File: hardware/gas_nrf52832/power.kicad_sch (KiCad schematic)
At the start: 31 parts, among them IC1 NPM1100-QDAA-R, J2 USB4515-GF-A_REVA, J3 Batt_SW, Q1 DMC2400UV

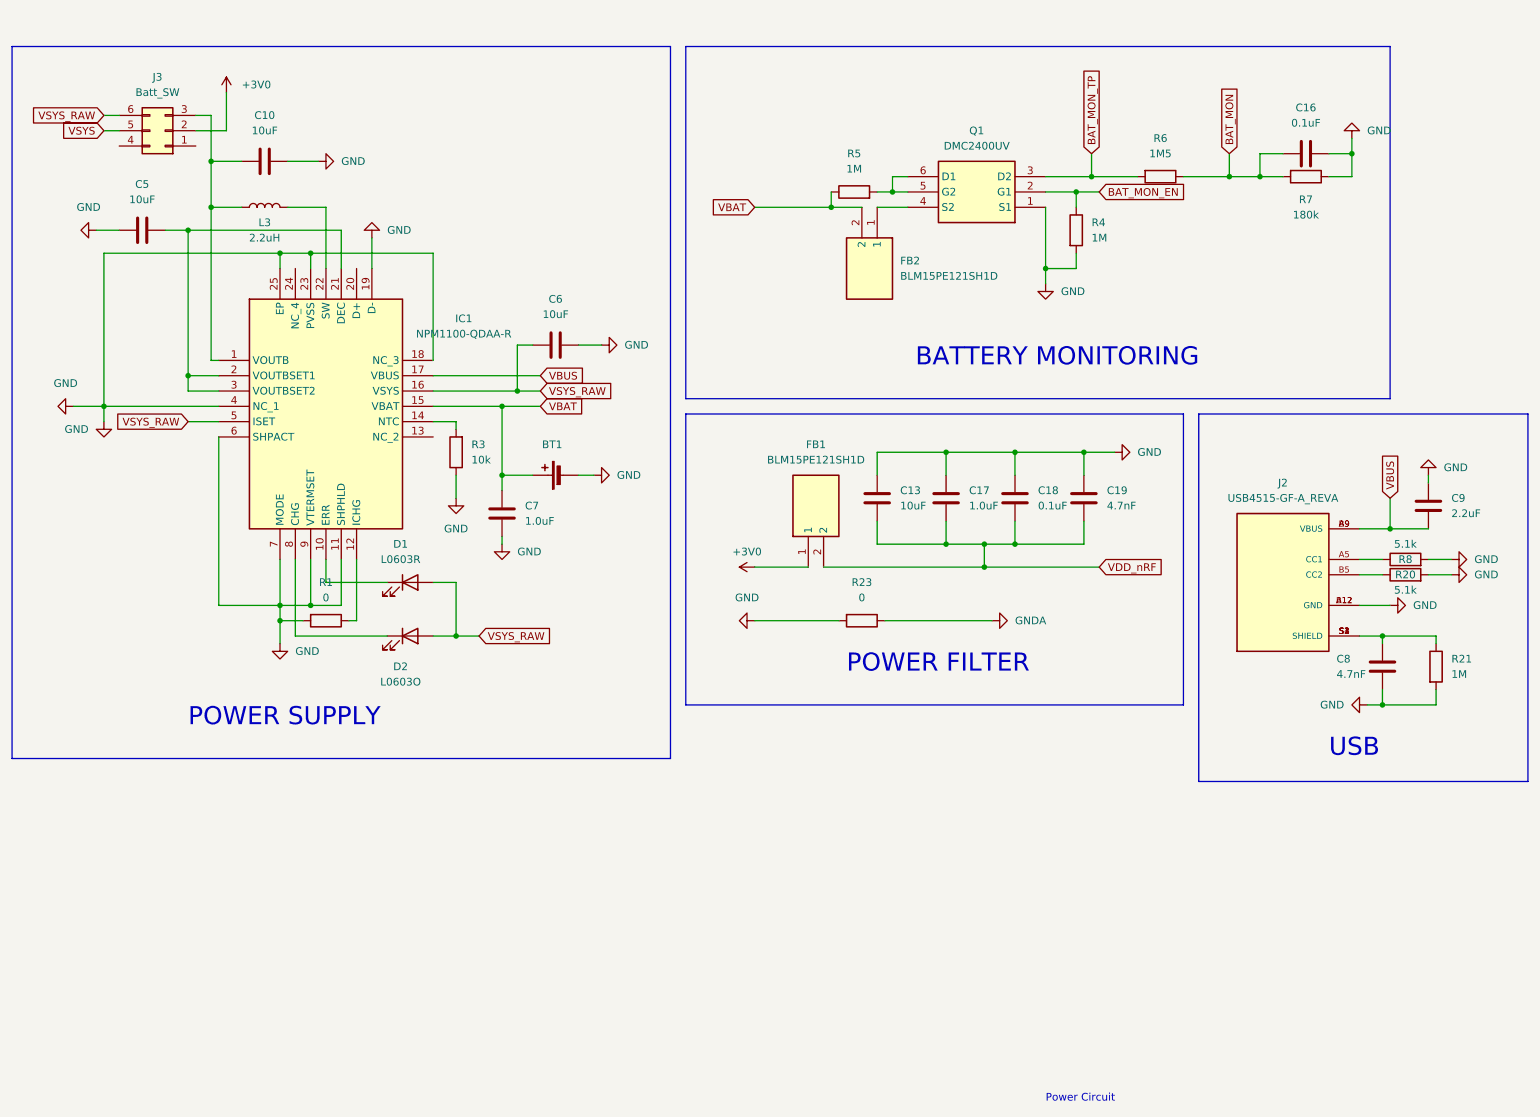
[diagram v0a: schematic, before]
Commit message: hw: fix sensor circuit & fix ERC Error
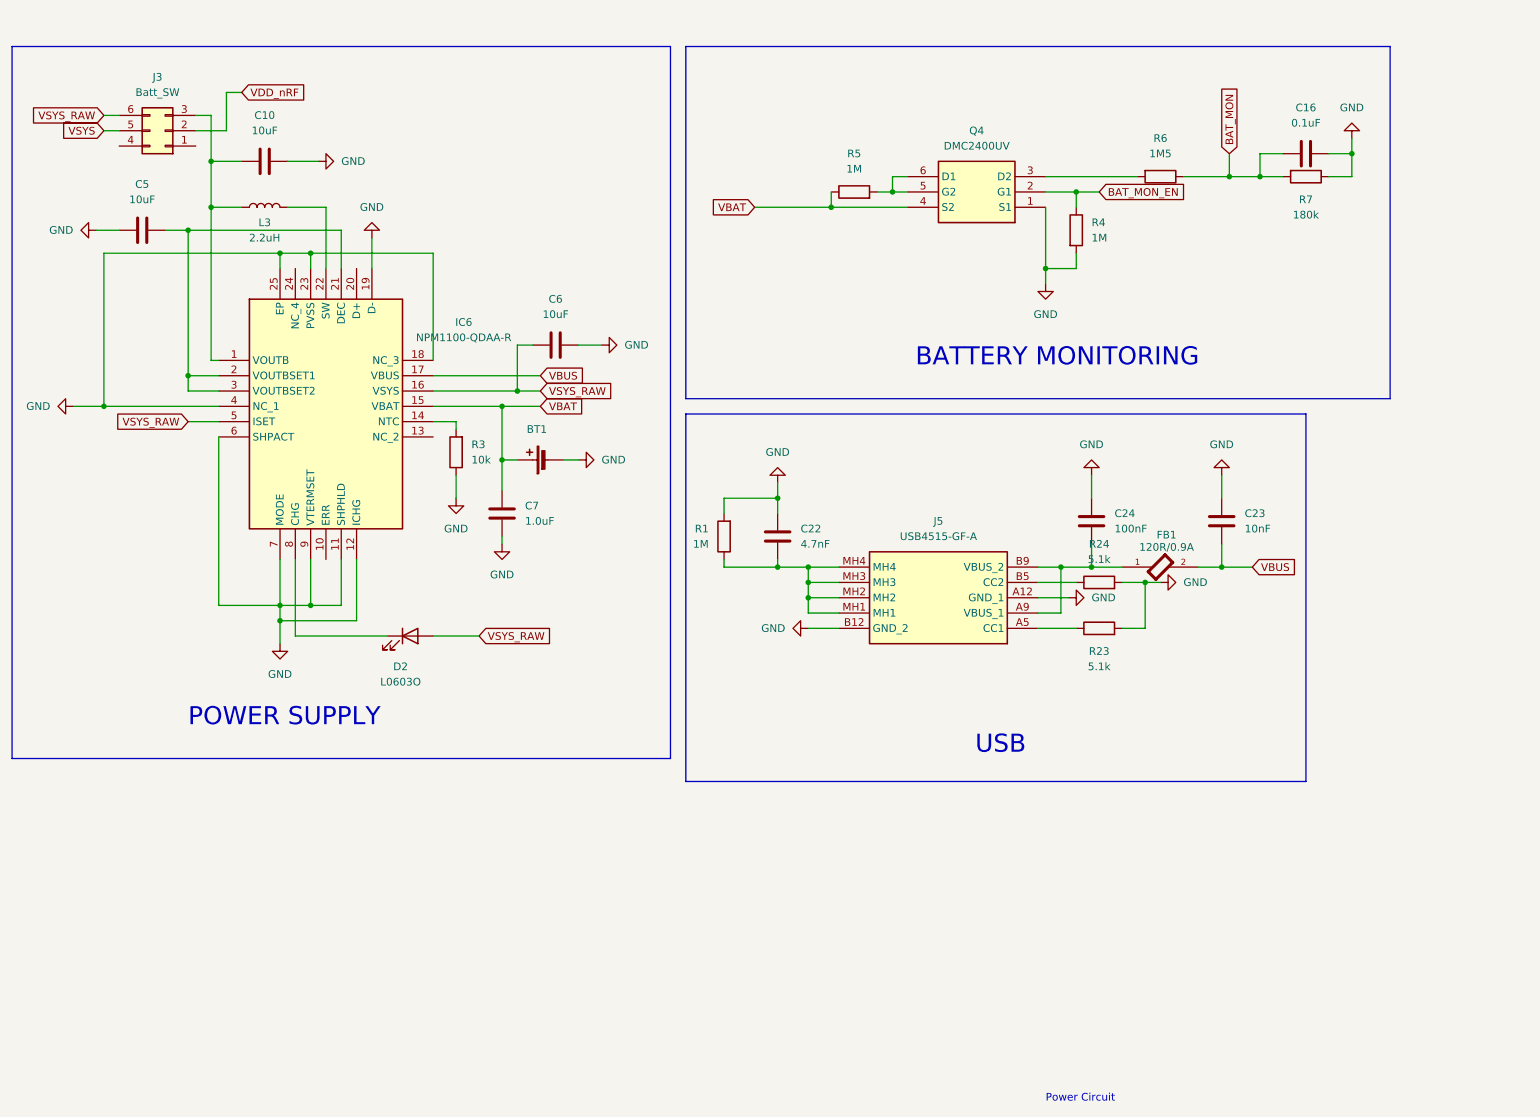
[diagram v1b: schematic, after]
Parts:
- removed C13: 10uF, Capacitor_SMD:C_0603_1608Metric, symbol Device:C
- removed C17: 1.0uF, Capacitor_SMD:C_0603_1608Metric, symbol Device:C
- removed C18: 0.1uF, Capacitor_SMD:C_0603_1608Metric, symbol Device:C
- removed C19, C8: 4.7nF, Capacitor_SMD:C_0402_1005Metric, symbol Device:C
- removed C9: 2.2uF, Capacitor_SMD:C_0603_1608Metric, symbol Device:C
- removed D1: L0603R, LED_SMD:LED_0603_1608Metric, symbol Device:LED
- removed FB1, FB2: BLM15PE121SH1D, BLM15PE121SH1D:NFZ15SG152SN10B, symbol Device:BLM15PE121SH1D
- removed IC1: NPM1100-QDAA-R, NPM1100-QDAA:QFN50P400X400X90-25N-D, symbol NPM1100-QDAA-R:NPM1100-QDAA-R
- removed J2: USB4515-GF-A_REVA, USB4515-GF-A_REVA:GCT_USB4515-GF-A_REVA, symbol USB4515-GF-A_REVA:USB4515-GF-A_REVA
- removed Q1: DMC2400UV, DMC2400UV:SOTFL50P162X60-6N, symbol DMC2400UV:DMC2400UV
- removed R20, R8: 5.1k, Resistor_SMD:R_0402_1005Metric, symbol Device:R
- removed R21: 1M, Resistor_SMD:R_0402_1005Metric, symbol Device:R
- added C22: 4.7nF, Capacitor_SMD:C_0402_1005Metric, symbol Device:C
- added C23: 10nF, Capacitor_SMD:C_0402_1005Metric, symbol Device:C
- added C24: 100nF, Capacitor_SMD:C_0402_1005Metric, symbol Device:C
- added FB1: 120R/0.9A, MURATA_BLM15PE121SH1D:MURATA_BLM15PE121SH1D_0, symbol MURATA_BLM15PE121SH1D:MURATA_BLM15PE121SH1D
- added IC6: NPM1100-QDAA-R, NPM1100-QDAA-R:QFN50P400X400X90-25N-D, symbol NPM1100-QDAA-R:NPM1100-QDAA-R
- added J5: USB4515-GF-A, USB4515-GF-A_REVA:USB4515GFA, symbol USB4515-GF-A:USB4515-GF-A
- added Q4: DMC2400UV, DMC2400UV:SOTFL50P162X60-6N, symbol DMC2400UV:DMC2400UV
- added R24: 5.1k, Resistor_SMD:R_0402_1005Metric, symbol Device:R
- C10, C16, C5, C6, C7: footprint Capacitor_SMD:C_0603_1608Metric -> Capacitor_SMD:C_0402_1005Metric
- R1: value 0 -> 1M
- R23: value 0 -> 5.1k
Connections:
- net +3V0 is gone; now on net VDD_nRF: J3.2 (Pin_2)
- net BAT_MON_EN: now also Q4.2 (G1)
- net GND: now also C22.1, C23.1, C24.1, IC6.11 (SHPHLD), IC6.12 (ICHG), IC6.18 (NC_3), IC6.19 (D-), IC6.23 (PVSS), IC6.25 (EP), IC6.4 (NC_1), IC6.6 (SHPACT), IC6.7 (MODE), IC6.9 (VTERMSET), J5.A12 (GND_1), J5.B12 (GND_2), Q4.1 (S1), R24.2
- net VBAT: now also IC6.15 (VBAT), Q4.4 (S2)
- net VBUS: now also C23.2, FB1.2, IC6.17 (VBUS)
- net VSYS_RAW: now also IC6.16 (VSYS), IC6.5 (ISET)
- net at C5.2: now also IC6.2 (VOUTBSET1), IC6.21 (DEC), IC6.3 (VOUTBSET2)
- net at R5.2: now also Q4.5 (G2), Q4.6 (D1)
- net at D2.1 (K): now also IC6.8 (CHG)
- net at C10.1, J3.3 (Pin_3), L3.1: now also IC6.1 (VOUTB)
- net at R1.1: now also C22.2, J5.MH1, J5.MH2, J5.MH3, J5.MH4
- net at R3.2: now also IC6.14 (NTC)
- net at L3.2: now also IC6.22 (SW)
- net BAT_MON_TP: no longer names the net of R6.2
- net BAT_MON_TP: now also Q4.3 (D2)
- net GNDA: no longer names the net of R23.1
- net GNDA: now also J5.A5 (CC1)
- new net: C24.2, FB1.1, J5.A9 (VBUS_1), J5.B9 (VBUS_2)
- new net: J5.B5 (CC2), R24.1
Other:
- note removed: "POWER FILTER"
- moved on the sheet: BT1

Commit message: feat: hw revision 1.0.2
Rev 1.0.2
- Oxygen Sensor
	- Voltage Amplification Ratio AdjustmentR18(10.7 -> 10k), R12(2.0k -> 2M)
	-> Reduce Current Consumption
	- Addition of lowpass filter for Noise Reduction
- Gas Sensor
	- Addition of lowpass filter for Noise Reduction
- 2 Layter -> 4 Layer
- hansam digitec requirement
	- If USB and RC are very close, errors may occur
	so increase the distance (R1, R23, R24, C22)
- BME680 Sensor Enable ctrl remove
- 32k Crystal Layout fix
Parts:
- removed C22: 4.7nF, Capacitor_SMD:C_0402_1005Metric, symbol Device:C
- removed R1: 1M, Resistor_SMD:R_0402_1005Metric, symbol Device:R
- added FB2: 120R/0.9A, MURATA_BLM15PE121SH1D:MURATA_BLM15PE121SH1D_0, symbol MURATA_BLM15PE121SH1D:MURATA_BLM15PE121SH1D
- C10, C5, C6: MANUFACTURER (none) -> Murata Electronics; Manufacturer_Part_Number (none) -> GRM155C80J106ME11D; Package (none) -> 0402 (1005 Metric); Type (none) -> Surface Mount
- C16: value 0.1uF -> 100nF; MANUFACTURER (none) -> Samsung Electro-Mechanics; Manufacturer_Part_Number (none) -> CL05B104KO5NNNC; Package (none) -> 0402 (1005 Metric); Type (none) -> Surface Mount
- C23: MANUFACTURER (none) -> Samsung Electro-Mechanics; Manufacturer_Part_Number (none) -> CL05B103KB5NNNC; Package (none) -> 0402 (1005 Metric); Type (none) -> Surface Mount
- C24: MANUFACTURER (none) -> Samsung Electro-Mechanics; Manufacturer_Part_Number (none) -> CL05B104KO5NNNC; Package (none) -> 0402 (1005 Metric); Type (none) -> Surface Mount
- C7: value 1.0uF -> 1uF; MANUFACTURER (none) -> Murata Electronics; Manufacturer_Part_Number (none) -> GRM155C71A105ME11D; Package (none) -> 0402 (1005 Metric); Type (none) -> Surface Mount
- D2: value L0603O -> L0603R; MANUFACTURER (none) -> BRIGHT LED; Manufacturer_Part_Number (none) -> BL-HUF36A-AV-TRB; Package (none) -> 0603 (1608 Metric); Type (none) -> Surface Mount
- FB1: MANUFACTURER (none) -> Murata Electronics; Manufacturer_Part_Number (none) -> BLM15PE121SH1D; Package None -> 0402 (1005 Metric); Type (none) -> Surface Mount
- IC6: MANUFACTURER (none) -> NORDIC SEMICONDUCTOR; Package (none) -> QFN-24(4x4); Type (none) -> Surface Mount
- J5: MANUFACTURER (none) -> Global Connector Technology; Type (none) -> Surface Mount
- L3: MANUFACTURER (none) -> Murata Electronics; Manufacturer_Part_Number (none) -> 1285AS-H-2R2M=P2; Package (none) -> 0806 (2016 Metric); Type (none) -> Surface Mount
- Q4: value DMC2400UV -> DMC2400UV-7; MANUFACTURER (none) -> Diodes Incorporated; Manufacturer_Part_Number DMC2400UV -> DMC2400UV-7; Package (none) -> SOT-563; Type (none) -> Surface Mount
- R23, R24: MANUFACTURER (none) -> TA-I Tech; Manufacturer_Part_Number (none) -> RM04FTN5101; Package (none) -> 0402 (1005 Metric); Type (none) -> Surface Mount
- R3: MANUFACTURER (none) -> TA-I Tech; Manufacturer_Part_Number (none) -> RM04FTN1002; Package (none) -> 0402 (1005 Metric); Type (none) -> Surface Mount
- R4, R5: MANUFACTURER (none) -> YAGEO; Manufacturer_Part_Number (none) -> RC0402FR-071ML; Package (none) -> 0402 (1005 Metric); Type (none) -> Surface Mount
- R6: MANUFACTURER (none) -> YAGEO; Manufacturer_Part_Number (none) -> RC0402FR-071M5L; Package (none) -> 0402 (1005 Metric); Type (none) -> Surface Mount
- R7: MANUFACTURER (none) -> TA-I Tech; Manufacturer_Part_Number (none) -> RM04FTN1803; Package (none) -> 0402 (1005 Metric); Type (none) -> Surface Mount
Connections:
- net VDD_nRF: now also J3.1 (Pin_1); no longer J3.2 (Pin_2)
- net VSYS: now also J3.4 (Pin_4); no longer J3.5 (Pin_5)
- net VSYS_RAW: now also J3.5 (Pin_5); no longer J3.6 (Pin_6)
- net at C10.1, IC6.1 (VOUTB), L3.1: now also FB2.1; no longer J3.3 (Pin_3)
- new net: FB2.2, J3.2 (Pin_2)
- now unconnected: J5.MH1, J5.MH2, J5.MH3, J5.MH4
- no-connect marks 0 -> 8
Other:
- moved on the sheet: BT1, C10, C5, C6, C7, D2, IC6, L3, R3

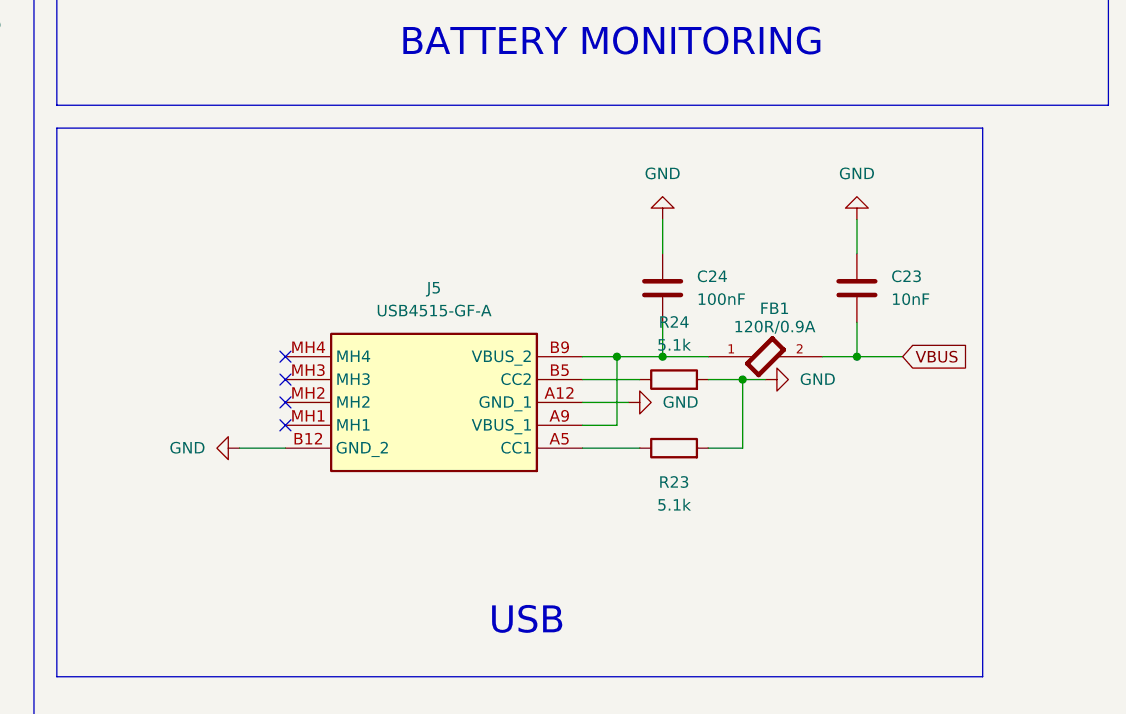
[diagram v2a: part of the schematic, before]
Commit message: feat: hw revision 1.0.3
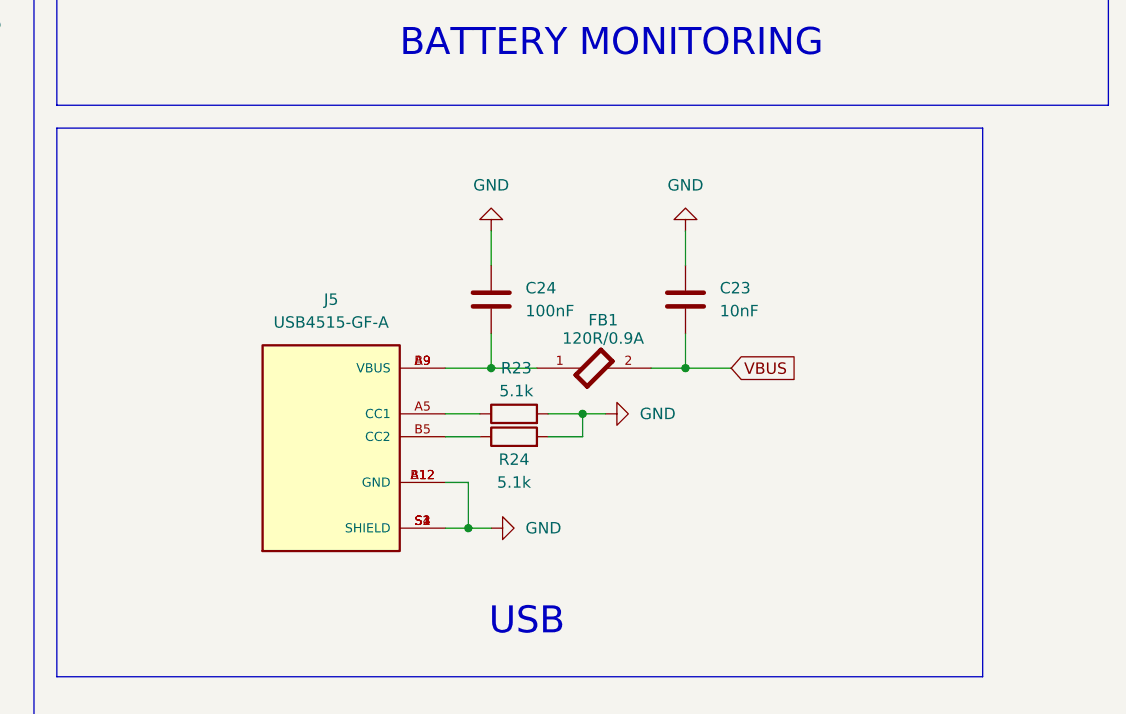
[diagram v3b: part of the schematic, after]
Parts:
- removed J5: USB4515-GF-A, USB4515-GF-A_REVA:USB4515GFA, symbol USB4515-GF-A:USB4515-GF-A
- added J5: USB4515-GF-A, USB4515-GF-A_REVA:GCT_USB4515-GF-A_REVA, symbol USB4515-GF-A_REVA:USB4515-GF-A_REVA
- renumbered R24 to R23, R23 to R24
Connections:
- net GND: now also J5.A12 (GND), J5.B12 (GND), J5.S1 (SHIELD), J5.S2 (SHIELD), J5.S3 (SHIELD), J5.S4 (SHIELD)
- net at R24.1: now also J5.B5 (CC2)
- net at C24.2, FB1.1: now also J5.A9 (VBUS), J5.B9 (VBUS)
- net at R23.1: now also J5.A5 (CC1)
- no-connect marks 8 -> 4
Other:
- moved on the sheet: C23, C24, FB1, R23, R24

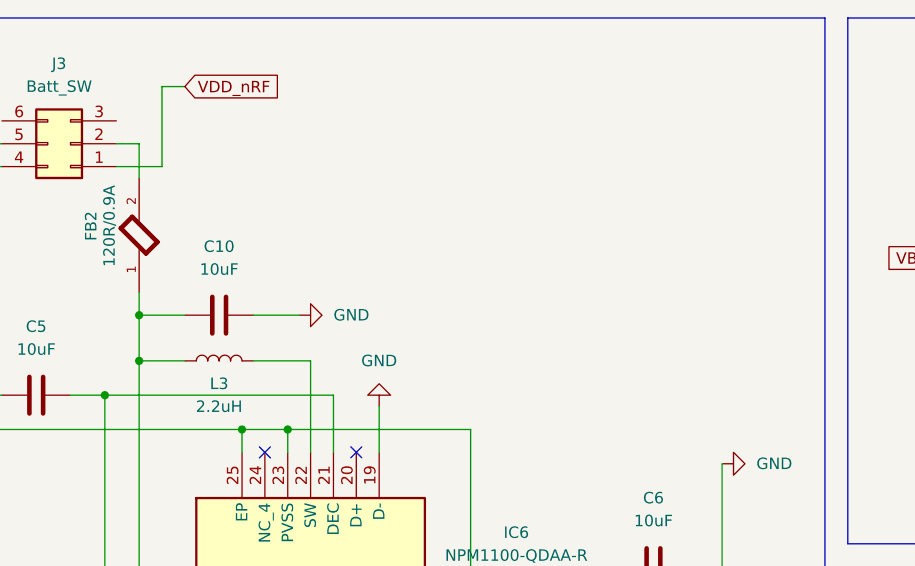
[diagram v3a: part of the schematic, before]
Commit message: test: gas biasing circuit
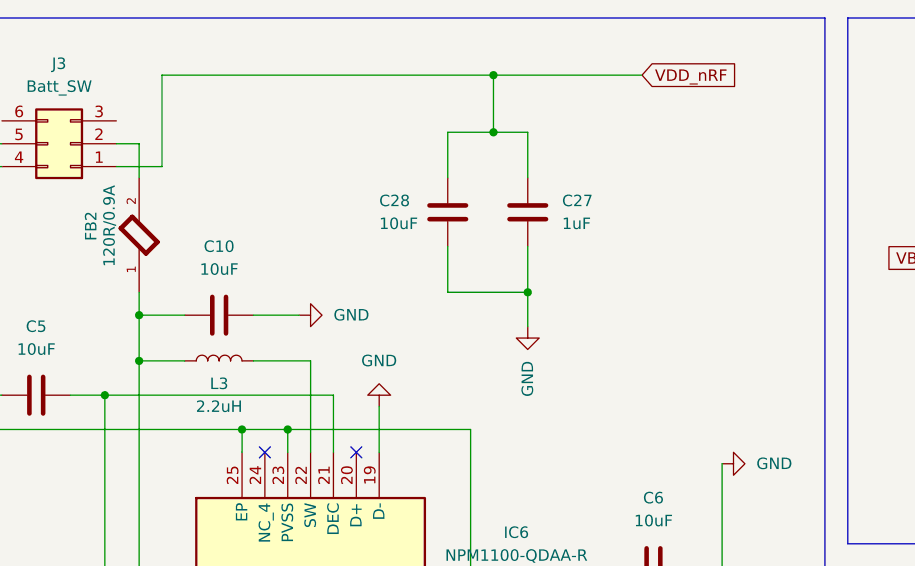
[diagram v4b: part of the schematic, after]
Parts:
- added C27: 1uF, Capacitor_SMD:C_0402_1005Metric, symbol Device:C
- added C28: 10uF, Capacitor_SMD:C_0402_1005Metric, symbol Device:C
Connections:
- net GND: now also C27.1, C28.1
- net VDD_nRF: now also C27.2, C28.2
